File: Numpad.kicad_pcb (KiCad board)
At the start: 2 copper layers, 76.2 x 97.6 mm, 51 parts, among them J1 USB_B_Mini, SW0 0, SW1 1, SW2 2, SW3 3, SW4 4, SW5 5, SW6 6, SW7 7, SW8 8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

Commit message: plate files added, moved around some more components
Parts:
- moved R3 97.2 mm to (197.7, 49.5), turned to 90 degrees
- moved R4 92.3 mm to (189.1, 97.4)
- moved C6 78.6 mm to (179.7, 97.4), turned to 180 degrees
- moved C5 75.6 mm to (179.7, 94.9), turned to 180 degrees
- moved C7 74.8 mm to (170.2, 106.6)
- moved C8 74.8 mm to (167.6, 106.6)
- moved C1 70.4 mm to (175.5, 119.6), turned to 270 degrees
- moved R2 69.4 mm to (194.6, 49.5), turned to 90 degrees
- moved R1 67.1 mm to (179.7, 119.8), turned to 270 degrees
- moved R5 59.0 mm to (160.7, 120.3), turned to 90 degrees
- moved C4 45.9 mm to (176.1, 85.0), turned to 90 degrees
- moved U1 5.24 mm to (168.1, 96.5)
- moved Y1 5.15 mm to (167.6, 84.9)
- moved C2 5.15 mm to (162.5, 84.9)
- moved C3 5.15 mm to (172.7, 84.9)
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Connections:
- U1 pad 10: Row3 -> Net-(U1-Pad10)
- U1 pad 11: Row4 -> Net-(U1-Pad11)
- U1 pad 18: Col1 -> Net-(U1-Pad18)
- U1 pad 19: Col2 -> Net-(U1-Pad19)
- U1 pad 20: Col3 -> Net-(U1-Pad20)
- U1 pad 21: Col4 -> Net-(U1-Pad21)
- U1 pad 25: Net-(U1-Pad25) -> Col4
- U1 pad 26: Net-(U1-Pad26) -> Col3
- U1 pad 28: Row5 -> Col2
- U1 pad 29: Net-(U1-Pad29) -> Col1
- U1 pad 37: Net-(U1-Pad37) -> Row5
- U1 pad 38: Net-(U1-Pad38) -> Row4
- U1 pad 39: Net-(U1-Pad39) -> Row3
- U1 pad 40: Net-(U1-Pad40) -> Row2
- U1 pad 41: Net-(U1-Pad41) -> Row1
- U1 pad 8: Row1 -> Net-(U1-Pad8)
- U1 pad 9: Row2 -> Net-(U1-Pad9)
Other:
- net class Power added: clearance 0.2, trace_width 0.381, via_dia 0.8, via_drill 0.4

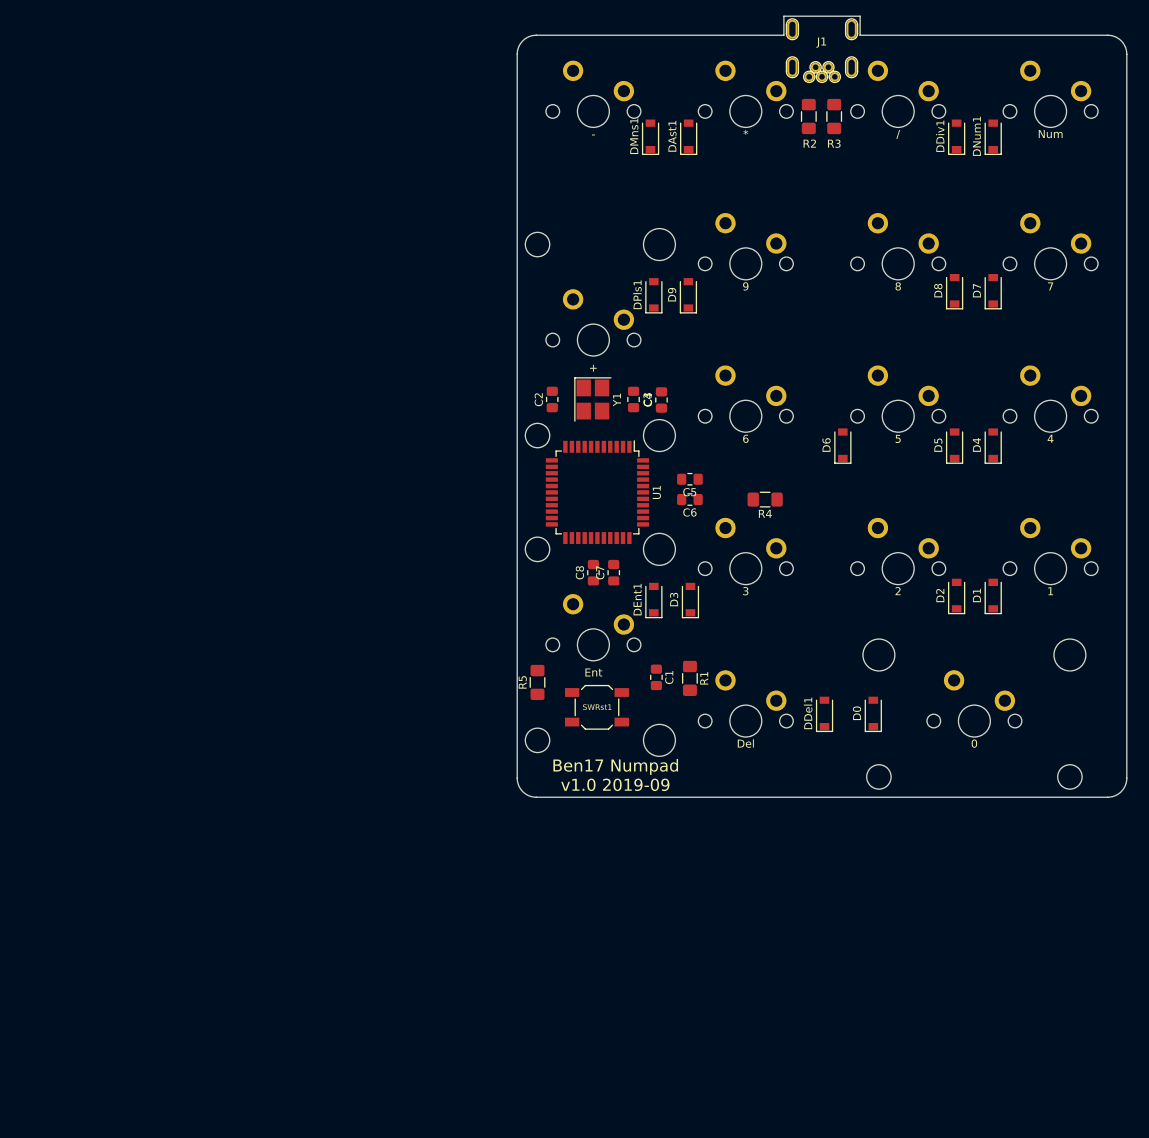
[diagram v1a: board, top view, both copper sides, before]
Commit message: added some traces, changed plate file
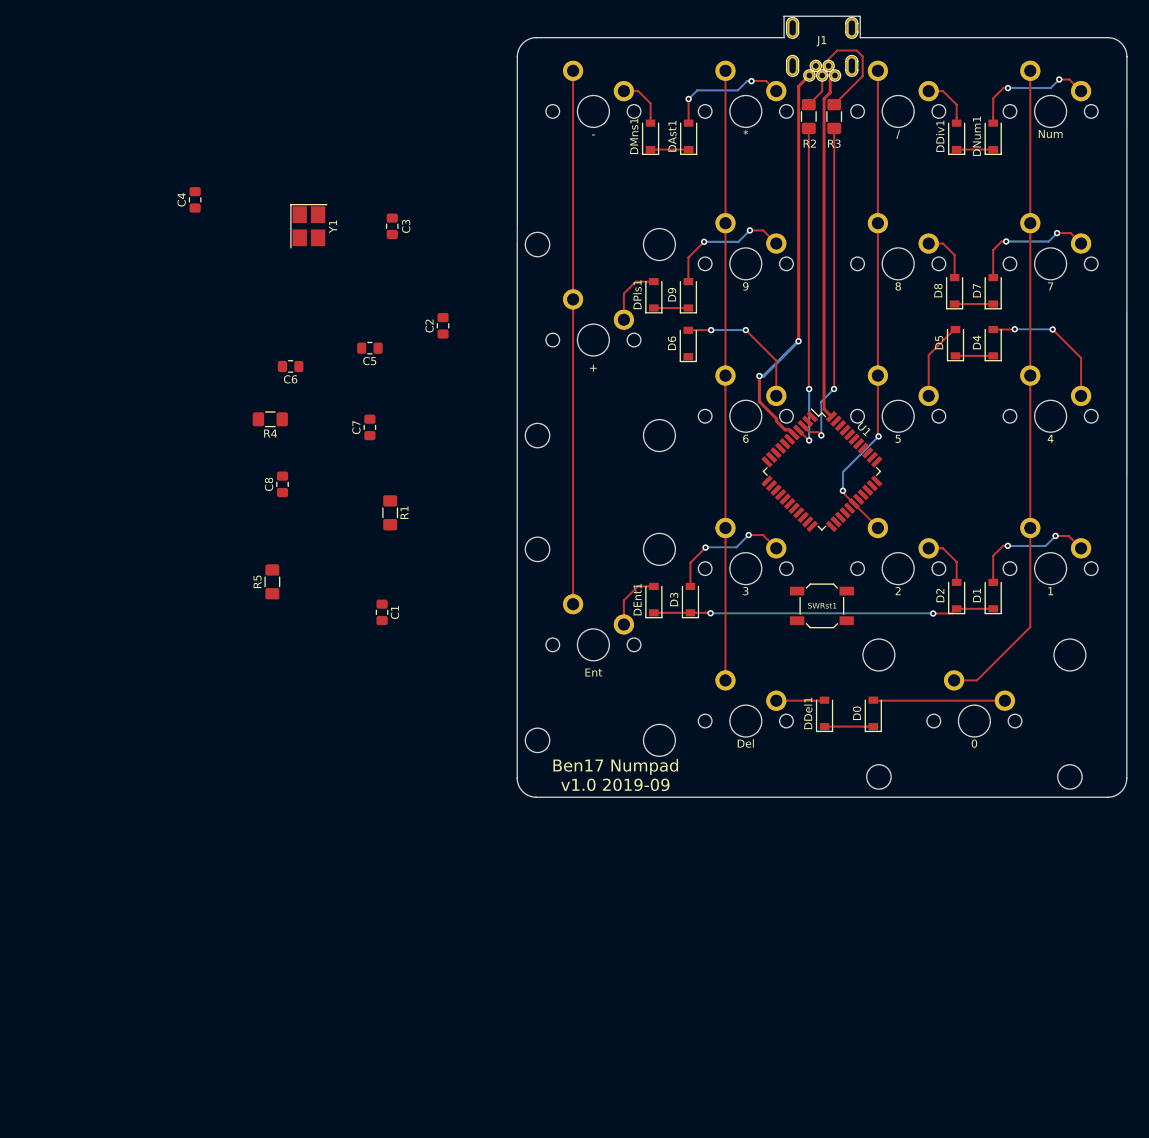
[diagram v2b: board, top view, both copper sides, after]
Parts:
- C6: value 0.1uF -> 1uF
- moved C4 63.4 mm to (117.9, 59.9)
- moved R4 62.7 mm to (127.3, 87.4)
- moved C6 52.6 mm to (129.8, 80.8)
- moved C5 43.2 mm to (139.7, 78.5)
- moved R1 42.8 mm to (142.2, 99.1)
- moved Y1 41.6 mm to (132.1, 63.2)
- moved C8 40.4 mm to (128.8, 95.5)
- moved C3 37.1 mm to (142.5, 63.2)
- moved C7 35.5 mm to (139.7, 88.4)
- moved R5 35.5 mm to (127.5, 107.7)
- moved C1 35.2 mm to (141.2, 111.5)
- moved SWRst1 30.8 mm to (196.2, 110.7)
- moved U1 28.2 mm to (196.2, 93.9), turned to 315 degrees
- moved D6 23.1 mm to (179.5, 77.9)
- moved C2 16.5 mm to (148.8, 75.7)
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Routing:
- net Col1: track 0.00 -> 81.8 mm
- net Col3: track 0.00 -> 76.2 mm
- net Col4: track 0.00 -> 66.7 mm
- net Col2: track 0.00 -> 60.8 mm, vias 0 -> 2
- net GND: track 0.00 -> 49.9 mm, vias 0 -> 2
- net +5V: track 0.00 -> 43.6 mm
- net Row4: track 0.00 -> 42.7 mm, vias 0 -> 2
- net D-: track 0.00 -> 41.8 mm, vias 0 -> 2
- net D+: track 0.00 -> 40.9 mm, vias 0 -> 2
- net Net-(D4-Pad2): track 0.00 -> 17.2 mm, vias 0 -> 2
- net Net-(D6-Pad2): track 0.00 -> 17.0 mm, vias 0 -> 2
- net Net-(D0-Pad2): track 0.00 -> 16.5 mm
- net Net-(D9-Pad2): track 0.00 -> 16.1 mm, vias 0 -> 2
- net Net-(D1-Pad2): track 0.00 -> 16.0 mm, vias 0 -> 2
- net Net-(D7-Pad2): track 0.00 -> 15.9 mm, vias 0 -> 2
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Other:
- outline, holes or cut-outs redrawn

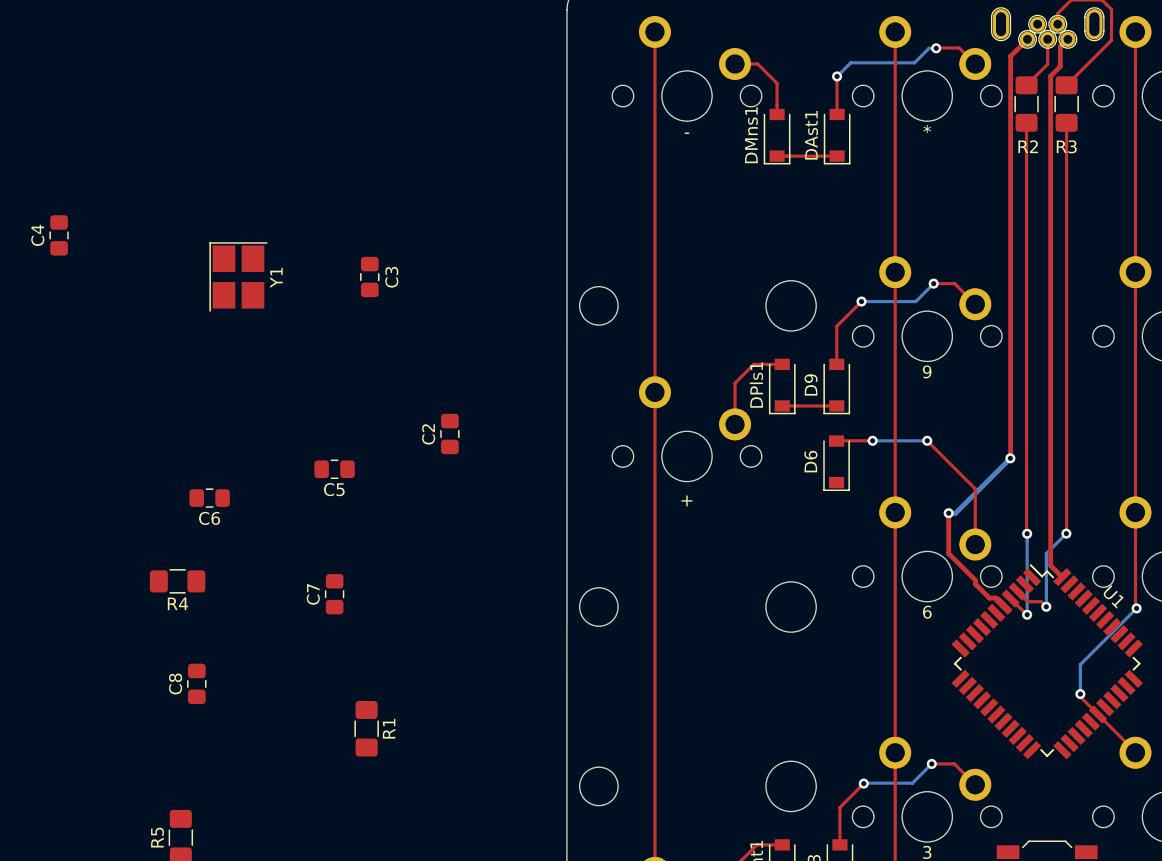
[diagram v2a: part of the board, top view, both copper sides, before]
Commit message: placed clock
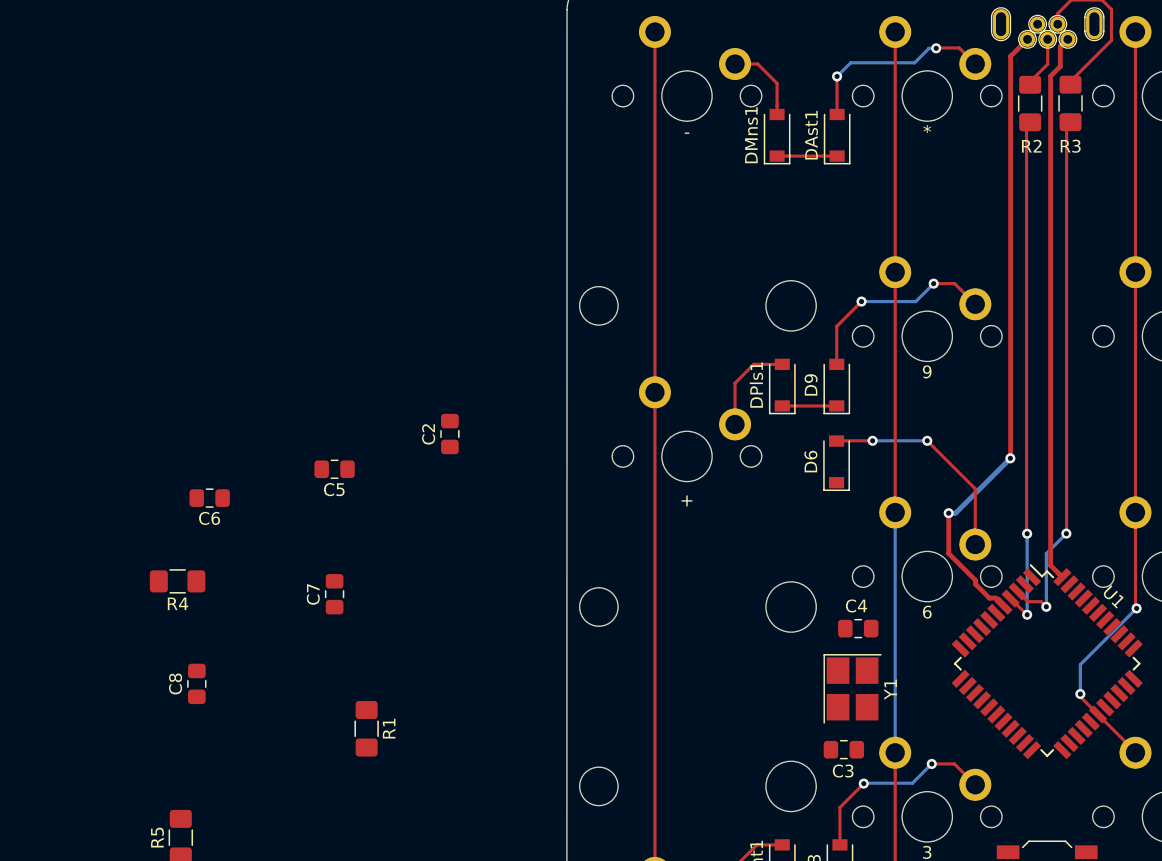
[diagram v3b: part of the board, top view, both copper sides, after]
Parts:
- moved C4 70.6 mm to (181.2, 91.1), turned to 180 degrees
- moved Y1 58.6 mm to (180.8, 95.9)
- moved C3 53.1 mm to (180.1, 100.7), turned to 180 degrees
- moved R3 0.31 mm to (198.1, 49.5)
- moved R2 0.29 mm to (194.8, 49.5)
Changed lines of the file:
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@@
     (thickness 1.6)
     (drawings 13)
-    (tracks 202)
+    (tracks 201)
     (zones 0)
     (modules 51)
@@
   )
   (module Crystal:Crystal_SMD_3225-4Pin_3.2x2.5mm_HandSoldering (layer F.Cu)
-    (at 132.08 63.246 270)
+    (at 180.77 95.9 270)
     (descr "SMD Crystal SERIES SMD3225/4 http://www.txccrystal.com/images/pdf/7m-accuracy.pdf, hand-soldering, 3.2x2.5mm^2 package")
     (tags "SMD SMT crystal hand-soldering")
@@
   )
   (module Resistor_SMD:R_1206_3216Metric_Pad1.42x1.75mm_HandSolder (layer F.Cu)
-    (at 197.739 49.53 90)
+    (at 198.05 49.48 90)
     (descr "Resistor SMD 1206 (3216 Metric), square (rectangular) end terminal, IPC_7351 nominal with elongated pad for handsoldering. (Body size source: http://www.tortai-tech.com/upload/download/2011102023233369053.pdf), generated with kicad-footprint-generator")
     (tags "resistor handsolder")
@@
   )
   (module Resistor_SMD:R_1206_3216Metric_Pad1.42x1.75mm_HandSolder (layer F.Cu)
-    (at 194.564 49.53 90)
+    (at 194.85 49.49 90)
     (descr "Resistor SMD 1206 (3216 Metric), square (rectangular) end terminal, IPC_7351 nominal with elongated pad for handsoldering. (Body size source: http://www.tortai-tech.com/upload/download/2011102023233369053.pdf), generated with kicad-footprint-generator")
     (tags "resistor handsolder")
@@
   )
   (module Capacitor_SMD:C_0805_2012Metric_Pad1.15x1.40mm_HandSolder (layer F.Cu)
-    (at 117.856 59.944 90)
+    (at 181.22 91.12 180)
     (descr "Capacitor SMD 0805 (2012 Metric), square (rectangular) end terminal, IPC_7351 nominal with elongated pad for handsoldering. (Body size source: https://docs.google.com/spreadsheets/d/1BsfQQcO9C6DZCsRaXUlFlo91Tg2WpOkGARC1WS5S8t0/edit?usp=sharing), generated with kicad-footprint-generator")
     (tags "capacitor handsolder")
     (attr smd)
-    (fp_text reference C4 (at 0 -1.65 90) (layer F.SilkS)
-      (effects (font (size 1 1) (thickness 0.15)))
-    )
-    (fp_text value 1uF (at 0 1.65 90) (layer F.Fab)
-      (effects (font (size 1 1) (thickness 0.15)))
-    )
-    (fp_text user %R (at 0 0 90) (layer F.Fab)
+    (fp_text reference C4 (at 0.14 1.76) (layer F.SilkS)
+      (effects (font (size 1 1) (thickness 0.15)))
+    )
+    (fp_text value 1uF (at 0 1.65) (layer F.Fab)
+      (effects (font (size 1 1) (thickness 0.15)))
+    )
+    (fp_text user %R (at 0 0) (layer F.Fab)
       (effects (font (size 0.5 0.5) (thickness 0.08)))
     )
@@
     (fp_line (start -1 -0.6) (end 1 -0.6) (layer F.Fab) (width 0.1))
     (fp_line (start -1 0.6) (end -1 -0.6) (layer F.Fab) (width 0.1))
-    (pad 2 smd roundrect (at 1.025 0 90) (size 1.15 1.4) (layers F.Cu F.Paste F.Mask) (roundrect_rratio 0.217391)
+    (pad 2 smd roundrect (at 1.025 0 180) (size 1.15 1.4) (layers F.Cu F.Paste F.Mask) (roundrect_rratio 0.217391)
       (net 1 GND))
-    (pad 1 smd roundrect (at -1.025 0 90) (size 1.15 1.4) (layers F.Cu F.Paste F.Mask) (roundrect_rratio 0.217391)
+    (pad 1 smd roundrect (at -1.025 0 180) (size 1.15 1.4) (layers F.Cu F.Paste F.Mask) (roundrect_rratio 0.217391)
       (net 5 "Net-(C4-Pad1)"))
     (model ${KISYS3DMOD}/Capacitor_SMD.3dshapes/C_0805_2012Metric.wrl
@@
   )
   (module Capacitor_SMD:C_0805_2012Metric_Pad1.15x1.40mm_HandSolder (layer F.Cu)
-    (at 142.494 63.246 90)
+    (at 180.08 100.72 180)
     (descr "Capacitor SMD 0805 (2012 Metric), square (rectangular) end terminal, IPC_7351 nominal with elongated pad for handsoldering. (Body size source: https://docs.google.com/spreadsheets/d/1BsfQQcO9C6DZCsRaXUlFlo91Tg2WpOkGARC1WS5S8t0/edit?usp=sharing), generated with kicad-footprint-generator")
     (tags "capacitor handsolder")
     (attr smd)
-    (fp_text reference C3 (at 0 1.778 90) (layer F.SilkS)
-      (effects (font (size 1 1) (thickness 0.15)))
-    )
-    (fp_text value 22pF (at 0 1.65 90) (layer F.Fab)
-      (effects (font (size 1 1) (thickness 0.15)))
-    )
-    (fp_text user %R (at 0 0 90) (layer F.Fab)
+    (fp_text reference C3 (at 0.04 -1.73) (layer F.SilkS)
+      (effects (font (size 1 1) (thickness 0.15)))
+    )
+    (fp_text value 22pF (at 0 1.65) (layer F.Fab)
+      (effects (font (size 1 1) (thickness 0.15)))
+    )
+    (fp_text user %R (at 0 0) (layer F.Fab)
       (effects (font (size 0.5 0.5) (thickness 0.08)))
     )
@@
     (fp_line (start -1 -0.6) (end 1 -0.6) (layer F.Fab) (width 0.1))
     (fp_line (start -1 0.6) (end -1 -0.6) (layer F.Fab) (width 0.1))
-    (pad 2 smd roundrect (at 1.025 0 90) (size 1.15 1.4) (layers F.Cu F.Paste F.Mask) (roundrect_rratio 0.217391)
+    (pad 2 smd roundrect (at 1.025 0 180) (size 1.15 1.4) (layers F.Cu F.Paste F.Mask) (roundrect_rratio 0.217391)
       (net 1 GND))
-    (pad 1 smd roundrect (at -1.025 0 90) (size 1.15 1.4) (layers F.Cu F.Paste F.Mask) (roundrect_rratio 0.217391)
+    (pad 1 smd roundrect (at -1.025 0 180) (size 1.15 1.4) (layers F.Cu F.Paste F.Mask) (roundrect_rratio 0.217391)
       (net 4 "Net-(C3-Pad1)"))
     (model ${KISYS3DMOD}/Capacitor_SMD.3dshapes/C_0805_2012Metric.wrl
@@
   (segment (start 213.75 79.45) (end 217.6145 79.45) (width 0.25) (layer F.Cu) (net 14))
   (segment (start 212.9 79.45) (end 213.75 79.45) (width 0.25) (layer F.Cu) (net 14))
+  (segment (start 200.230509 89.869491) (end 200.160509 89.869491) (width 0.25) (layer F.Cu) (net 14))
   (segment (start 212.75 76.15) (end 212.9 76.15) (width 0.25) (layer F.Cu) (net 15))
   (segment (start 209.55 79.35) (end 212.75 76.15) (width 0.25) (layer F.Cu) (net 15))
@@
   (segment (start 203.2 43.815) (end 203.2 45.611051) (width 0.25) (layer F.Cu) (net 35))
   (segment (start 203.2 62.865) (end 203.2 81.915) (width 0.25) (layer F.Cu) (net 35))
-  (segment (start 200.230509 89.869491) (end 200.160509 89.869491) (width 0.25) (layer F.Cu) (net 14))
   (via (at 203.29 89.52) (size 0.8) (drill 0.4) (layers F.Cu B.Cu) (net 35))
   (segment (start 203.2 81.915) (end 203.2 89.43) (width 0.25) (layer F.Cu) (net 35))
@@
   (segment (start 200.230509 97.930509) (end 203.2 100.9) (width 0.25) (layer F.Cu) (net 35))
   (segment (start 184.15 43.815) (end 184.15 62.865) (width 0.25) (layer F.Cu) (net 36))
-  (segment (start 184.15 83.711051) (end 184.15 100.965) (width 0.25) (layer F.Cu) (net 36))
-  (segment (start 184.15 81.915) (end 184.15 83.711051) (width 0.25) (layer F.Cu) (net 36))
   (segment (start 184.15 102.761051) (end 184.15 120.015) (width 0.25) (layer F.Cu) (net 36))
   (segment (start 184.15 100.965) (end 184.15 102.761051) (width 0.25) (layer F.Cu) (net 36))
   (segment (start 184.15 62.865) (end 184.15 81.915) (width 0.25) (layer F.Cu) (net 36))
+  (segment (start 184.15 100.965) (end 184.15 81.915) (width 0.25) (layer B.Cu) (net 36))
   (segment (start 165.1 43.815) (end 165.1 72.39) (width 0.25) (layer F.Cu) (net 37))
   (segment (start 165.1 110.49) (end 165.1 72.39) (width 0.25) (layer F.Cu) (net 37))
